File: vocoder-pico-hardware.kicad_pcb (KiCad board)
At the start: 2 copper layers, 47 x 108 mm, 70 parts, among them J1 Conn_02x05_Odd_Even, J2 AudioJack2_SwitchT, J3 AudioJack2_SwitchT, Q1 BC547, Q2 BC547, Q3 BC547, Q4 BC547, SW1 SW_Push, SW2 SW_Push, U1 TL072, U2 LM7805_TO220, U3 PCM5100A, U4 SC39-11GWA, U5 SC39-11GWA, U6 SC39-11GWA, U7 SC39-11GWA, U8 MCP6002-xP

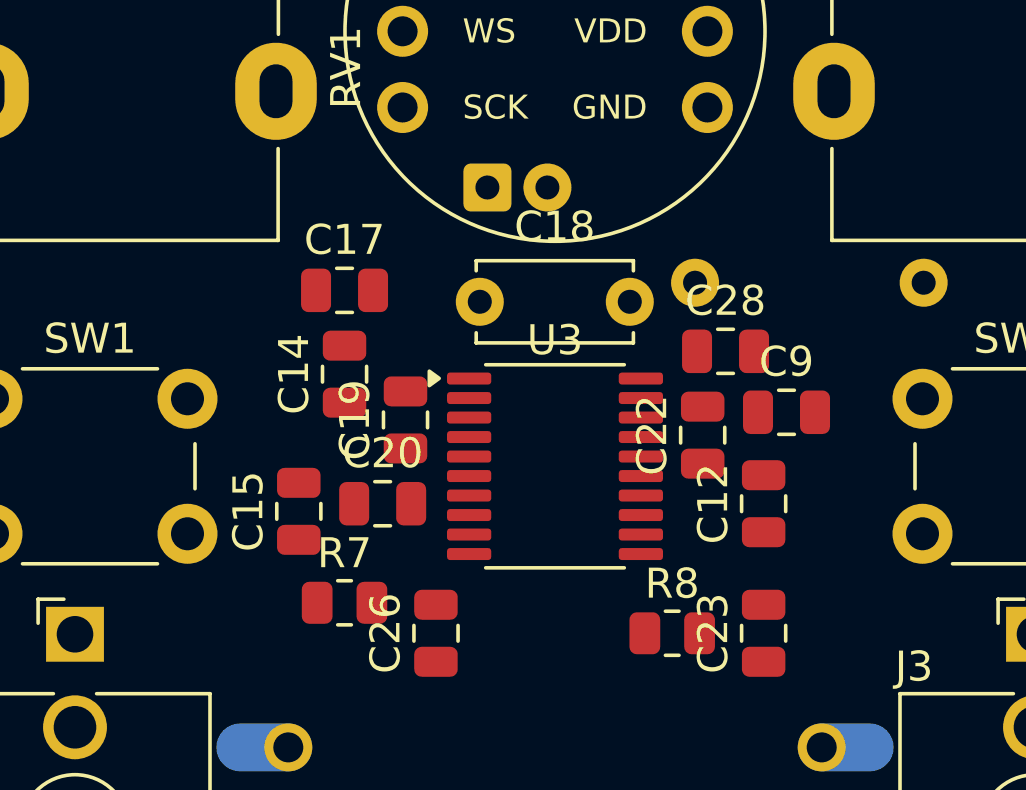
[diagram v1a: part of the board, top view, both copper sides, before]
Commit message: begin routing of DAC
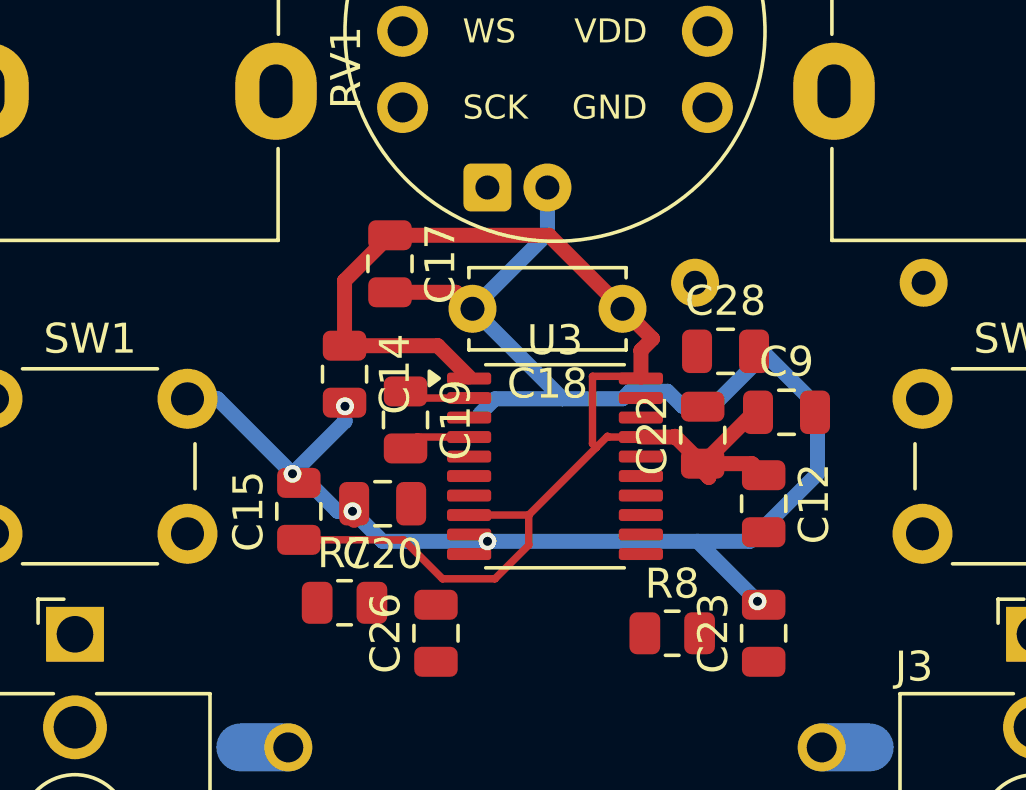
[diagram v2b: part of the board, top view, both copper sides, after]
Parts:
- moved C18 4.76 mm to (79.8, 72.8), turned to 180 degrees
- moved C17 1.76 mm to (72.0, 71.2), turned to -90 degrees
- turned C12 to -90 degrees
- turned C14 to -90 degrees
- turned C19 to -90 degrees
- turned C20 to 180 degrees
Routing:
- net GND: track 0.00 -> 59.3 mm, vias 0 -> 5
- net Vdd: track 0.00 -> 49.4 mm
- net Net-(U3-CAPM): track 0.00 -> 2.28 mm
- net Net-(U3-CAPP): track 0.00 -> 2.21 mm

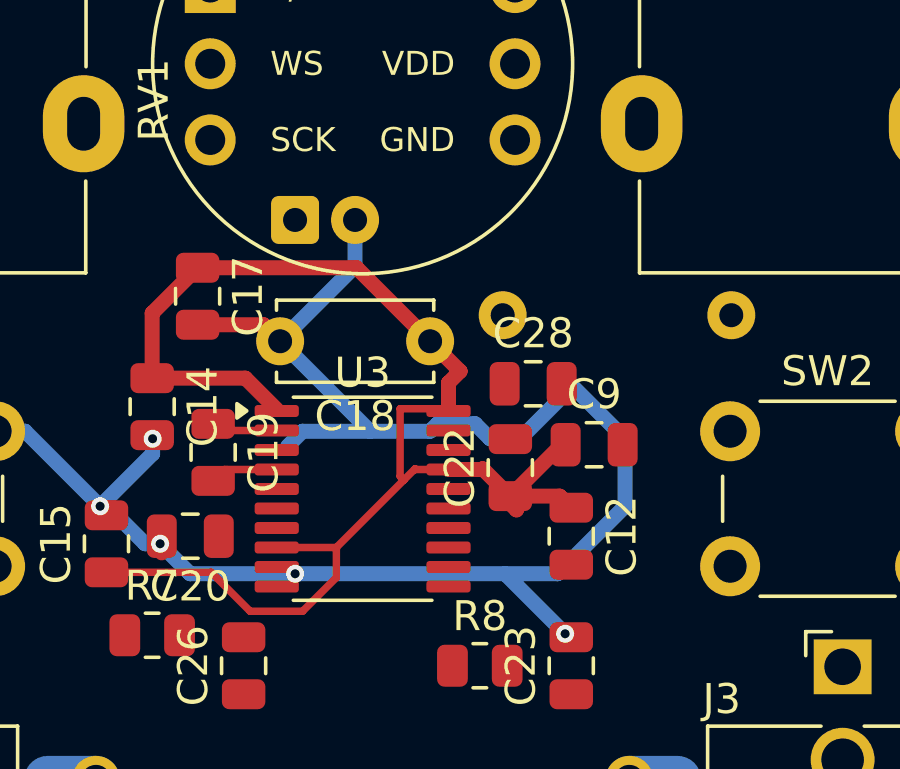
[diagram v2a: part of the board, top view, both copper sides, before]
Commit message: reposition C22
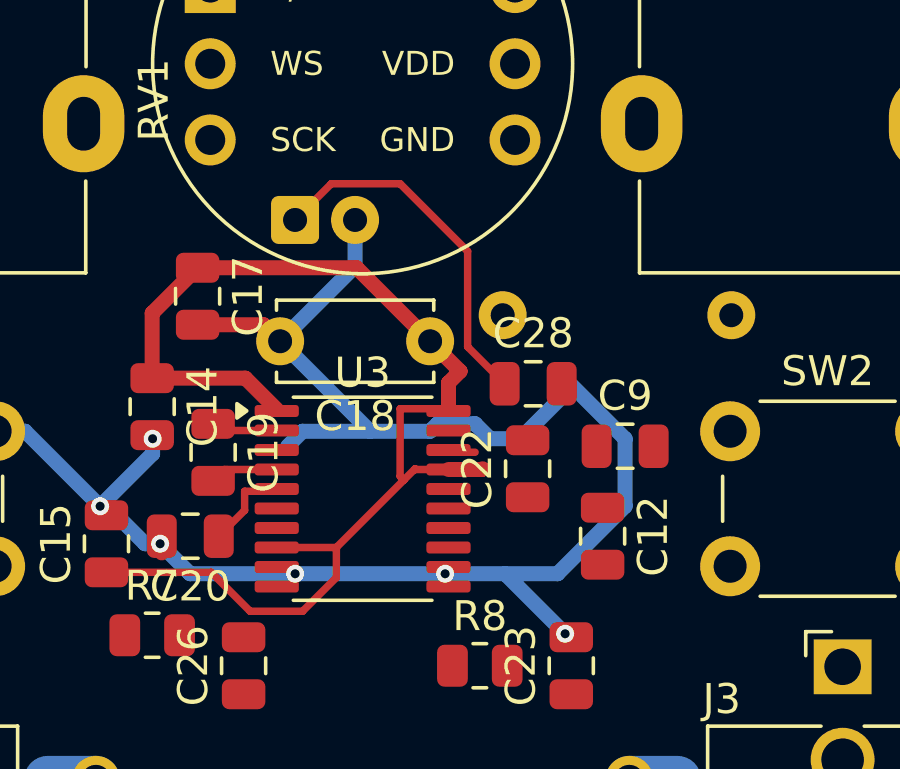
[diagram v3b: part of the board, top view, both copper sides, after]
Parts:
- moved C12 1.05 mm to (85.5, 79.2)
- moved C9 1.03 mm to (86.2, 76.2)
- moved C22 0.58 mm to (83.0, 77.0)
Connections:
- U3 pad 7: Net-(U3-OUTR) -> unconnected-(U3-OUTR-Pad7)
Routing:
- net Net-(U3-LDOO): track 0.00 -> 13.0 mm
- net Vdd: track 49.4 -> 42.2 mm
- net Net-(U3-VNEG): track 0.00 -> 2.96 mm
- net GND: vias 5 -> 6

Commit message: continue routing the dac
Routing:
- net Vdd: track 42.2 -> 48.9 mm
- net GND: track 59.3 -> 60.3 mm, vias 6 -> 10
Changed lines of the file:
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@@
+	)
+	(segment
+		(start 74.6375 76.375)
+		(end 75.625 76.375)
+		(width 0.25)
+		(layer "F.Cu")
+		(net 1)
 	)
 	(segment
@@
 	)
 	(segment
+		(start 75.625 76.375)
+		(end 76.25 75.75)
+		(width 0.25)
+		(layer "F.Cu")
+		(net 1)
+	)
+	(segment
 		(start 74.2 72.2)
 		(end 74.75 72.75)
@@
 	)
 	(via
+		(at 84.5 74.25)
+		(size 0.6)
+		(drill 0.3)
+		(layers "F.Cu" "B.Cu")
+		(net 1)
+	)
+	(via
+		(at 82.875 75.875)
+		(size 0.6)
+		(drill 0.3)
+		(layers "F.Cu" "B.Cu")
+		(net 1)
+	)
+	(via
 		(at 68.75 78.25)
 		(size 0.6)
@@
 	)
 	(via
+		(at 85.75 80.25)
+		(size 0.6)
+		(drill 0.3)
+		(layers "F.Cu" "B.Cu")
+		(net 1)
+	)
+	(via
 		(at 75.25 80.5)
+		(size 0.6)
+		(drill 0.3)
+		(layers "F.Cu" "B.Cu")
+		(net 1)
+	)
+	(via
+		(at 76.25 75.75)
 		(size 0.6)
 		(drill 0.3)
@@
 	)
 	(segment
-		(start 84 80.5)
-		(end 86.25 78.25)
+		(start 84.25 74.5)
+		(end 82.875 75.875)
 		(width 0.5)
 		(layer "B.Cu")
@@
 	)
 	(segment
-		(start 86.25 78.25)
+		(start 85.75 80.25)
+		(end 86.25 79.75)
+		(width 0.5)
+		(layer "B.Cu")
+		(net 1)
+	)
+	(segment
+		(start 86.25 76)
+		(end 84.5 74.25)
+		(width 0.5)
+		(layer "B.Cu")
+		(net 1)
+	)
+	(segment
+		(start 79.75 75.75)
+		(end 77.75 75.75)
+		(width 0.5)
+		(layer "B.Cu")
+		(net 1)
+	)
+	(segment
+		(start 86.25 79.75)
 		(end 86.25 76)
+		(width 0.5)
+		(layer "B.Cu")
+		(net 1)
+	)
+	(segment
+		(start 84.25 74)
+		(end 84.25 74.5)
+		(width 0.5)
+		(layer "B.Cu")
+		(net 1)
+	)
+	(segment
+		(start 75.25 80.5)
+		(end 80.25 80.5)
+		(width 0.5)
+		(layer "B.Cu")
+		(net 1)
+	)
+	(segment
+		(start 68.75 78.25)
+		(end 70.5 76.5)
+		(width 0.5)
+		(layer "B.Cu")
+		(net 1)
+	)
+	(segment
+		(start 77.75 75.75)
+		(end 74.75 72.75)
+		(width 0.5)
+		(layer "B.Cu")
+		(net 1)
+	)
+	(segment
+		(start 85.5 80.5)
+		(end 85.75 80.25)
+		(width 0.5)
+		(layer "B.Cu")
+		(net 1)
+	)
+	(segment
+		(start 77.75 75.75)
+		(end 76.25 75.75)
+		(width 0.5)
+		(layer "B.Cu")
+		(net 1)
+	)
+	(segment
+		(start 80.25 80.5)
+		(end 82.25 80.5)
+		(width 0.5)
+		(layer "B.Cu")
+		(net 1)
+	)
+	(segment
+		(start 81.25 75.5)
+		(end 80 75.5)
+		(width 0.5)
+		(layer "B.Cu")
+		(net 1)
+	)
+	(segment
+		(start 80 75.5)
+		(end 79.75 75.75)
 		(width 0.5)
 		(layer "B.Cu")
@@
 	)
 	(segment
-		(start 75.25 80.5)
-		(end 80.25 80.5)
-		(width 0.5)
-		(layer "B.Cu")
-		(net 1)
-	)
-	(segment
-		(start 68.75 78.25)
-		(end 70.5 76.5)
-		(width 0.5)
-		(layer "B.Cu")
-		(net 1)
-	)
-	(segment
-		(start 77.75 75.75)
-		(end 74.75 72.75)
-		(width 0.5)
-		(layer "B.Cu")
-		(net 1)
-	)
-	(segment
-		(start 84.25 74)
-		(end 84.25 74.5)
-		(width 0.5)
-		(layer "B.Cu")
-		(net 1)
-	)
-	(segment
-		(start 77.75 75.75)
-		(end 75.5 75.75)
-		(width 0.5)
-		(layer "B.Cu")
-		(net 1)
-	)
-	(segment
-		(start 80.25 80.5)
-		(end 82.25 80.5)
-		(width 0.5)
-		(layer "B.Cu")
-		(net 1)
-	)
-	(segment
-		(start 80 75.5)
-		(end 79.75 75.75)
-		(width 0.5)
-		(layer "B.Cu")
-		(net 1)
-	)
-	(segment
-		(start 81.25 75.5)
-		(end 80 75.5)
-		(width 0.5)
-		(layer "B.Cu")
-		(net 1)
-	)
-	(segment
-		(start 75.5 75.75)
-		(end 75 76.25)
-		(width 0.5)
-		(layer "B.Cu")
-		(net 1)
-	)
-	(segment
 		(start 74.75 72.75)
 		(end 77.2475 70.2525)
@@
 	)
 	(segment
-		(start 79.75 75.75)
-		(end 77.75 75.75)
-		(width 0.5)
-		(layer "B.Cu")
-		(net 1)
-	)
-	(segment
 		(start 84.25 82.5)
 		(end 84.75 82.5)
@@
 	)
 	(segment
-		(start 84.25 74.5)
-		(end 82.75 76)
+		(start 82.5 80.5)
+		(end 85.5 80.5)
+		(width 0.5)
+		(layer "B.Cu")
+		(net 1)
+	)
+	(segment
+		(start 84.5 74.25)
+		(end 84.25 74)
 		(width 0.5)
 		(layer "B.Cu")
@@
 	)
 	(segment
+		(start 68.75 78.25)
+		(end 66.25 75.75)
+		(width 0.5)
+		(layer "B.Cu")
+		(net 1)
+	)
+	(segment
+		(start 82.875 75.875)
+		(end 82.75 76)
+		(width 0.5)
+		(layer "B.Cu")
+		(net 1)
+	)
+	(segment
+		(start 66.25 75.75)
+		(end 65.25 75.75)
+		(width 0.5)
+		(layer "B.Cu")
+		(net 1)
+	)
+	(segment
 		(start 81.75 76)
 		(end 81.25 75.5)
@@
 	)
 	(segment
-		(start 68.75 78.25)
-		(end 66.25 75.75)
-		(width 0.5)
-		(layer "B.Cu")
-		(net 1)
-	)
-	(segment
-		(start 66.25 75.75)
-		(end 65.25 75.75)
-		(width 0.5)
-		(layer "B.Cu")
-		(net 1)
-	)
-	(segment
-		(start 82.25 80.5)
-		(end 84 80.5)
-		(width 0.5)
-		(layer "B.Cu")
-		(net 1)
-	)
-	(segment
 		(start 70.5 76.5)
 		(end 70.5 76)
@@
 	)
 	(segment
-		(start 86.25 76)
-		(end 84.25 74)
-		(width 0.5)
-		(layer "B.Cu")
-		(net 1)
+		(start 85.5 76.45)
+		(end 85.3 76.25)
+		(width 0.5)
+		(layer "F.Cu")
+		(net 20)
 	)
 	(segment
@@
 	)
 	(segment
+		(start 81.475 77.025)
+		(end 82.075 77.025)
+		(width 0.5)
+		(layer "F.Cu")
+		(net 20)
+	)
+	(segment
 		(start 70.485 73.98)
 		(end 70.485 71.815)
@@
 	)
 	(segment
+		(start 78.75 75)
+		(end 78.75 77.25)
+		(width 0.25)
+		(layer "F.Cu")
+		(net 20)
+	)
+	(segment
+		(start 81.475 77.025)
+		(end 80.3625 77.025)
+		(width 0.5)
+		(layer "F.Cu")
+		(net 20)
+	)
+	(segment
+		(start 81.5 77)
+		(end 81.475 77.025)
+		(width 0.5)
+		(layer "F.Cu")
+		(net 20)
+	)
+	(segment
+		(start 78.875 77.375)
+		(end 79.25 77)
+		(width 0.25)
+		(layer "F.Cu")
+		(net 20)
+	)
+	(segment
+		(start 85.5 78.298)
+		(end 85.5 76.45)
+		(width 0.5)
+		(layer "F.Cu")
+		(net 20)
+	)
+	(segment
+		(start 79.25 77)
+		(end 79.275 77.025)
+		(width 0.25)
+		(layer "F.Cu")
+		(net 20)
+	)
+	(segment
+		(start 80.3625 74.1375)
+		(end 80.3625 75.025)
+		(width 0.5)
+		(layer "F.Cu")
+		(net 20)
+	)
+	(segment
 		(start 72.452 80.452)
 		(end 73.75 81.75)
@@
 	)
 	(segment
-		(start 78.75 75)
-		(end 78.75 77.25)
-		(width 0.25)
-		(layer "F.Cu")
-		(net 20)
-	)
-	(segment
-		(start 81.475 77.025)
-		(end 80.3625 77.025)
-		(width 0.5)
-		(layer "F.Cu")
-		(net 20)
-	)
-	(segment
-		(start 81.5 77)
-		(end 81.475 77.025)
-		(width 0.5)
-		(layer "F.Cu")
-		(net 20)
-	)
-	(segment
-		(start 78.875 77.375)
-		(end 79.25 77)
-		(width 0.25)
-		(layer "F.Cu")
-		(net 20)
-	)
-	(segment
-		(start 79.25 77)
-		(end 79.275 77.025)
-		(width 0.25)
-		(layer "F.Cu")
-		(net 20)
-	)
-	(segment
-		(start 80.3625 74.1375)
-		(end 80.3625 75.025)
-		(width 0.5)
-		(layer "F.Cu")
-		(net 20)
-	)
-	(segment
 		(start 78.75 77.25)
 		(end 78.875 77.375)
@@
 	)
 	(segment
+		(start 83 77.95)
+		(end 85.152 77.95)
+		(width 0.5)
+		(layer "F.Cu")
+		(net 20)
+	)
+	(segment
 		(start 80.3625 75.075)
 		(end 80.2875 75)
@@
 	)
 	(segment
+		(start 85.152 77.95)
+		(end 85.5 78.298)
+		(width 0.5)
+		(layer "F.Cu")
+		(net 20)
+	)
+	(segment
 		(start 68.961 80.452)
 		(end 72.452 80.452)
@@
 		(layer "F.Cu")
 		(net 20)
+	)
+	(segment
+		(start 82.075 77.025)
+		(end 83 77.95)
+		(width 0.5)
+		(layer "F.Cu")
+		(net 20)

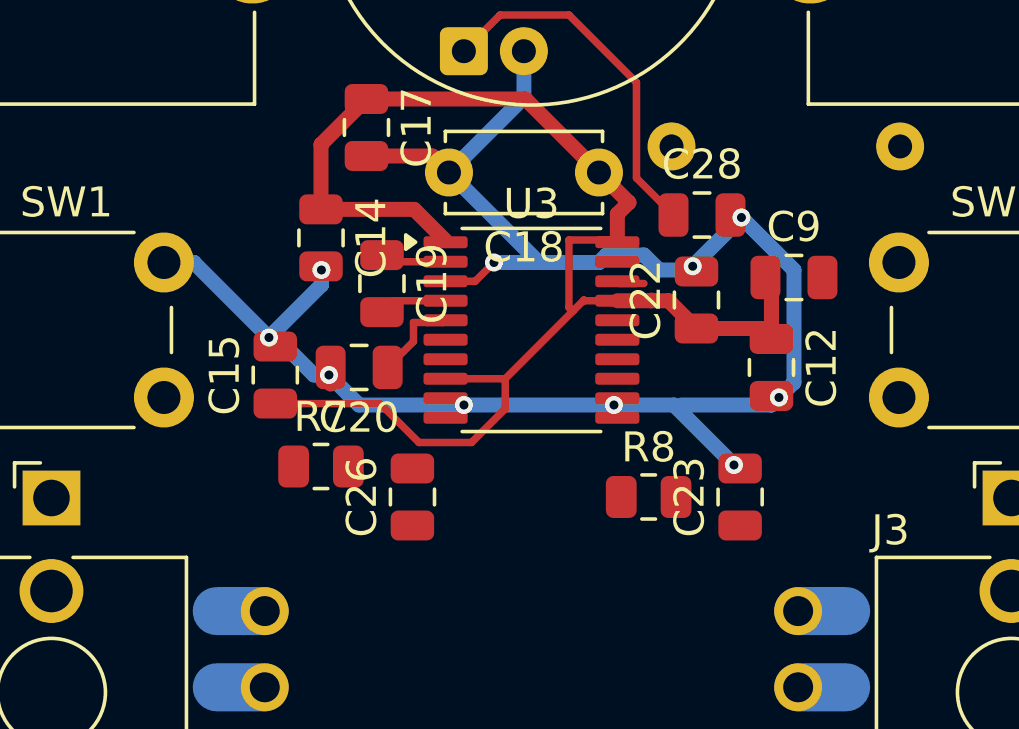
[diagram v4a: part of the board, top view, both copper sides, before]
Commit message: finish routing the dac section
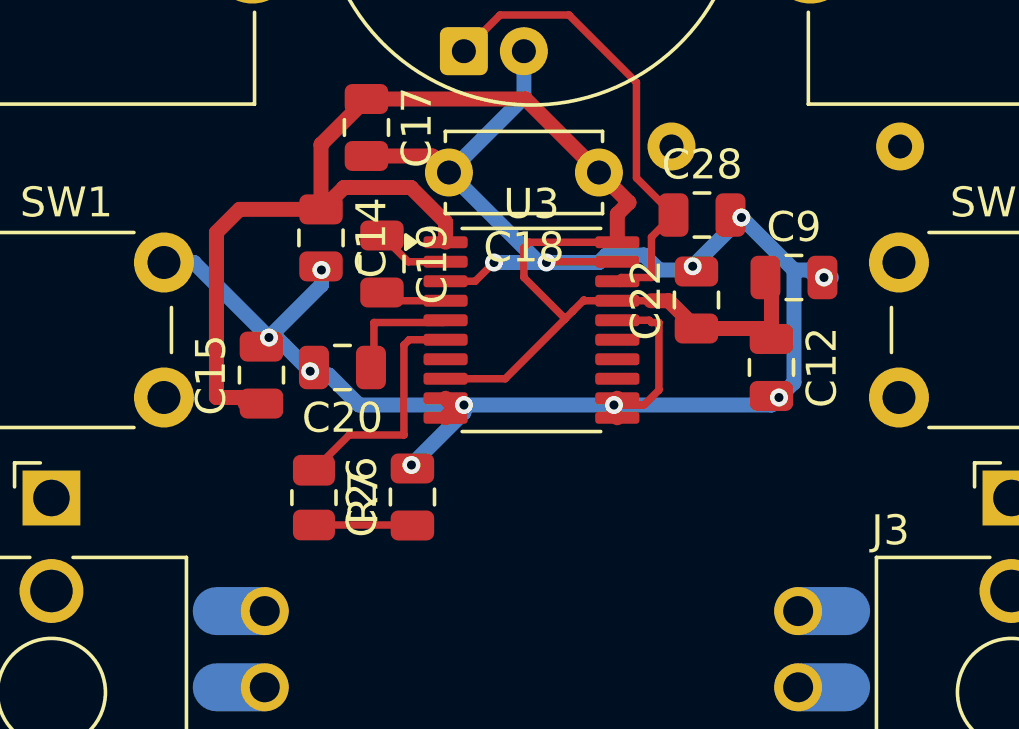
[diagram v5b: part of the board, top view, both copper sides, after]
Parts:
- removed C23: 2.2nf, Capacitor_SMD:C_0805_2012Metric
- removed R8: 470Ohm, Resistor_SMD:R_0805_2012Metric
- moved R7 1.06 mm to (70.2, 83.6), turned to -90 degrees
- moved C19 0.65 mm to (72.5, 75.8)
- moved C20 0.56 mm to (71.2, 79.2)
- moved C15 0.46 mm to (68.5, 79.5)
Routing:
- net GND: track 60.3 -> 70.7 mm, vias 10 -> 12
- net Net-(U3-OUTL): track 0.00 -> 7.95 mm
- net Vdd: track 48.9 -> 54.3 mm
- net OUtL: track 0.00 -> 3.29 mm
- net Net-(U3-LDOO): track 13.0 -> 15.8 mm
- net Net-(U3-VNEG): track 2.96 -> 4.31 mm
